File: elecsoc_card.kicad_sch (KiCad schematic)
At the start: 22 parts, among them J1 Conn_01x02_Pin, J2 Conn_01x02_Pin, U1 NA555D

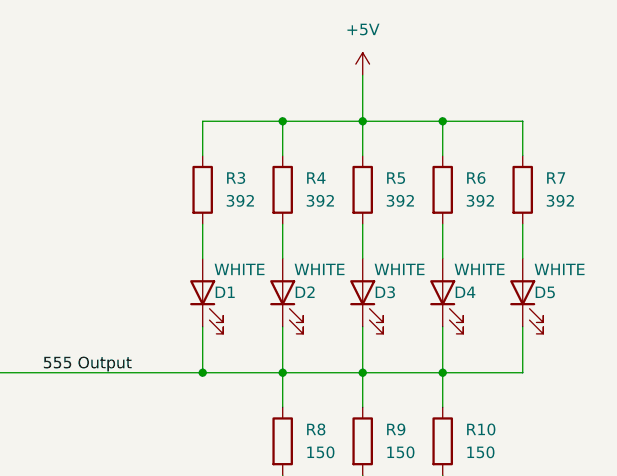
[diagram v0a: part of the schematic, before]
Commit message: Changed R3-R7 to 390
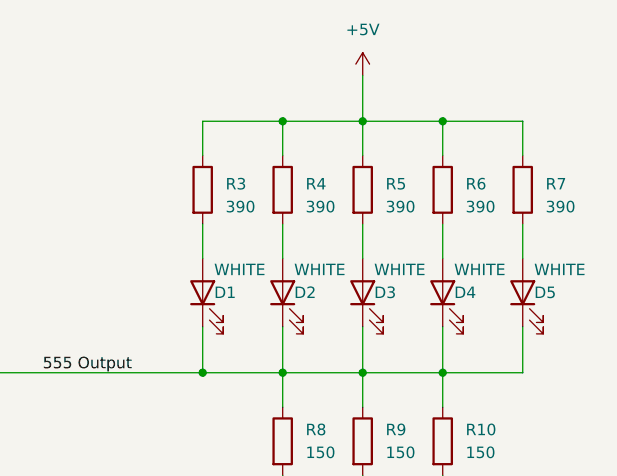
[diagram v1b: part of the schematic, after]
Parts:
- R3, R4, R5, R6, R7: value 392 -> 390
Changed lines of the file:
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@@
   (symbol (lib_id "Device:R") (at 146.05 71.12 0) (unit 1)
     (in_bom yes) (on_board yes) (dnp no) (fields_autoplaced)
-    (property "Reference" "R3" (at 148.59 69.85 0)
-      (effects (font (size 1.27 1.27)) (justify left))
-    )
-    (property "Value" "392" (at 148.59 72.39 0)
+    (property "Reference" "R3" (at 148.59 70.485 0)
+      (effects (font (size 1.27 1.27)) (justify left))
+    )
+    (property "Value" "390" (at 148.59 73.025 0)
       (effects (font (size 1.27 1.27)) (justify left))
     )
@@
   (symbol (lib_id "Device:R") (at 163.83 71.12 0) (unit 1)
     (in_bom yes) (on_board yes) (dnp no) (fields_autoplaced)
-    (property "Reference" "R5" (at 166.37 69.85 0)
-      (effects (font (size 1.27 1.27)) (justify left))
-    )
-    (property "Value" "392" (at 166.37 72.39 0)
+    (property "Reference" "R5" (at 166.37 70.485 0)
+      (effects (font (size 1.27 1.27)) (justify left))
+    )
+    (property "Value" "390" (at 166.37 73.025 0)
       (effects (font (size 1.27 1.27)) (justify left))
     )
@@
   (symbol (lib_id "Device:R") (at 172.72 71.12 0) (unit 1)
     (in_bom yes) (on_board yes) (dnp no) (fields_autoplaced)
-    (property "Reference" "R6" (at 175.26 69.85 0)
-      (effects (font (size 1.27 1.27)) (justify left))
-    )
-    (property "Value" "392" (at 175.26 72.39 0)
+    (property "Reference" "R6" (at 175.26 70.485 0)
+      (effects (font (size 1.27 1.27)) (justify left))
+    )
+    (property "Value" "390" (at 175.26 73.025 0)
       (effects (font (size 1.27 1.27)) (justify left))
     )
@@
   (symbol (lib_id "Device:R") (at 181.61 71.12 0) (unit 1)
     (in_bom yes) (on_board yes) (dnp no) (fields_autoplaced)
-    (property "Reference" "R7" (at 184.15 69.85 0)
-      (effects (font (size 1.27 1.27)) (justify left))
-    )
-    (property "Value" "392" (at 184.15 72.39 0)
+    (property "Reference" "R7" (at 184.15 70.485 0)
+      (effects (font (size 1.27 1.27)) (justify left))
+    )
+    (property "Value" "390" (at 184.15 73.025 0)
       (effects (font (size 1.27 1.27)) (justify left))
     )
@@
   (symbol (lib_id "Device:R") (at 154.94 71.12 0) (unit 1)
     (in_bom yes) (on_board yes) (dnp no) (fields_autoplaced)
-    (property "Reference" "R4" (at 157.48 69.85 0)
-      (effects (font (size 1.27 1.27)) (justify left))
-    )
-    (property "Value" "392" (at 157.48 72.39 0)
-      (effects (font (size 1.27 1.27)) (justify left))
-    )
+    (property "Reference" "R4" (at 157.48 70.485 0)
+      (effects (font (size 1.27 1.27)) (justify left))
+    )
+    (property "Value" "390" (at 157.48 73.025 0)
+      (effects (font (size 1.27 1.27)) (justify left))
+    )

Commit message: SchematicCleanup
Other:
- note added: "Oscillator Circ."
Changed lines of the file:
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@@
     (fill (type none))
   )
-  (text "Frontside USB Connector" (at 34.29 81.28 0)
+  (rectangle (start 77.47 71.12) (end 93.98 109.22)
+    (stroke (width 0) (type default))
+    (fill (type none))
+  )
+  (text "Frontside USB Connector" (at 57.15 81.28 0)
+    (effects (font (size 1.27 1.27)) (justify right bottom))
+  )
+  (text "T = 0.693*(R1+2*R2)*C1\n  = 0.693 * 3 * 4.99k * 47u \n  = 0.487s"
+    (at 66.04 127 0)
     (effects (font (size 1.27 1.27)) (justify left bottom))
   )
-  (text "T = 0.693*(R1+2*R2)*C1\n  = 0.693 * 3 * 4.99k * 47u \n  = 0.487s"
-    (at 66.04 125.73 0)
+  (text "Backside USB Connector" (at 57.15 110.49 0)
+    (effects (font (size 1.27 1.27)) (justify right bottom))
+  )
+  (text "Oscillator\nCirc." (at 93.98 114.3 0)
+    (effects (font (size 1.27 1.27)) (justify right bottom))
+  )
+  (text "Resistors and capacitance values for oscillator" (at 66.04 119.38 0)
     (effects (font (size 1.27 1.27)) (justify left bottom))
   )
-  (text "Backside USB Connector" (at 34.29 110.49 0)
-    (effects (font (size 1.27 1.27)) (justify left bottom))
-  )
-  (text "Resistors and capacitance values for oscillator" (at 66.04 118.11 0)
-    (effects (font (size 1.27 1.27)) (justify left bottom))
-  )

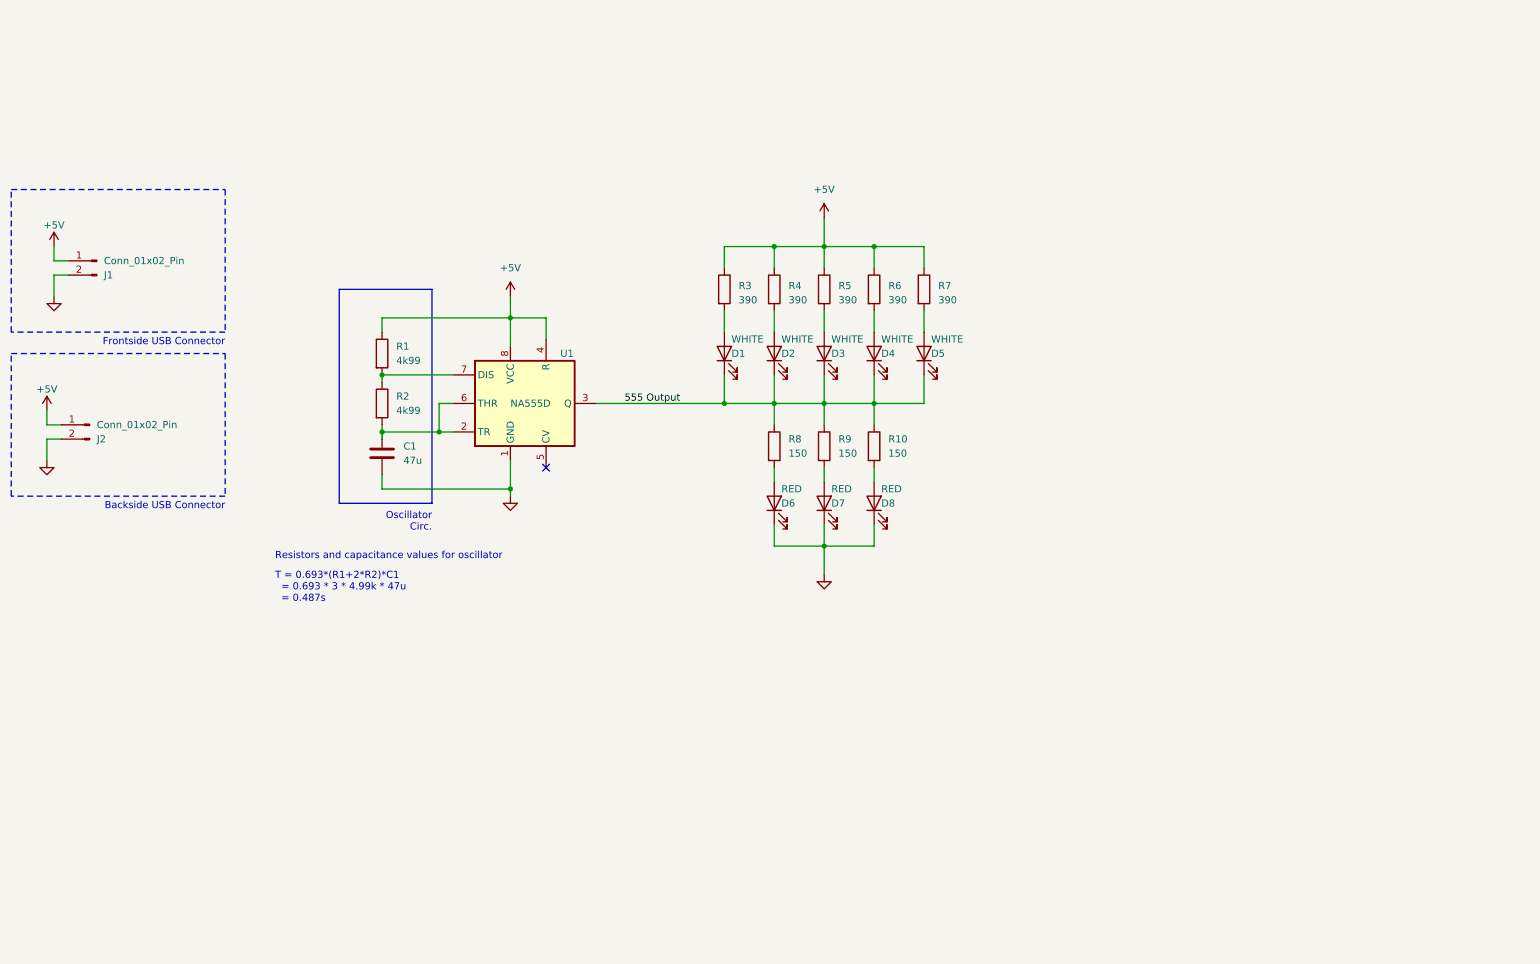
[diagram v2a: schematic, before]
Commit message: Removed Items for Rev2, for Daniel to complete
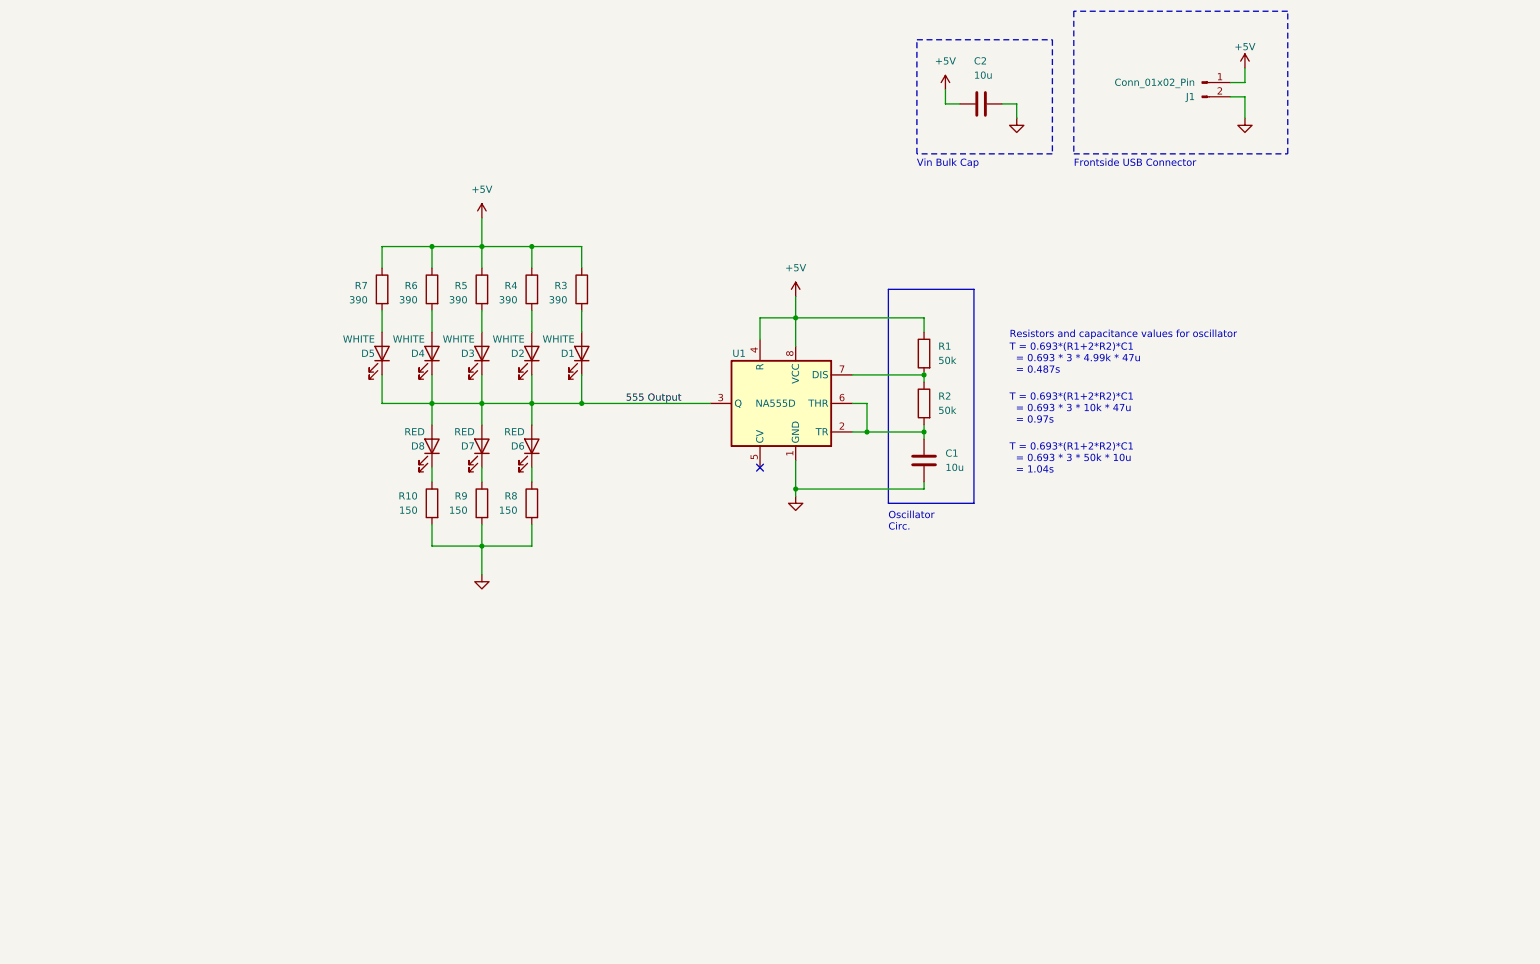
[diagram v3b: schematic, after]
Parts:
- removed J2: Conn_01x02_Pin, Library:USB_A_Male_inboard, symbol Connector:Conn_01x02_Pin
- added C2: 10u, Capacitor_SMD:C_0805_2012Metric_Pad1.18x1.45mm_HandSolder, symbol Device:C
- C1: value 47u -> 10u
- D8: Mfr. No: (none) -> IN-S85AT5UW
- R1, R2: value 4k99 -> 50k
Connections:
- net +5V: now also C2.1
- net 555 Output: now also D6.2 (A), D7.2 (A), D8.2 (A); no longer R10.1, R8.1, R9.1
- net GND: now also R10.2, R8.2, R9.2, C2.2; no longer D6.1 (K), D7.1 (K), D8.1 (K)
- new net: D8.1 (K), R10.1
- new net: D6.1 (K), R8.1
- new net: D7.1 (K), R9.1
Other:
- note added: "T = 0.693*(R1+2*R2)*C1 = 0.693 * 3 * 10k * 47u = 0.97s"
- note added: "T = 0.693*(R1+2*R2)*C1 = 0.693 * 3 * 50k * 10u = 1.04s"
- note added: "Vin Bulk Cap"
- note removed: "Backside USB Connector"
- moved on the sheet: C1, D1, D2, D3, D4, D5, D6, D7, D8, J1, R1, R10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

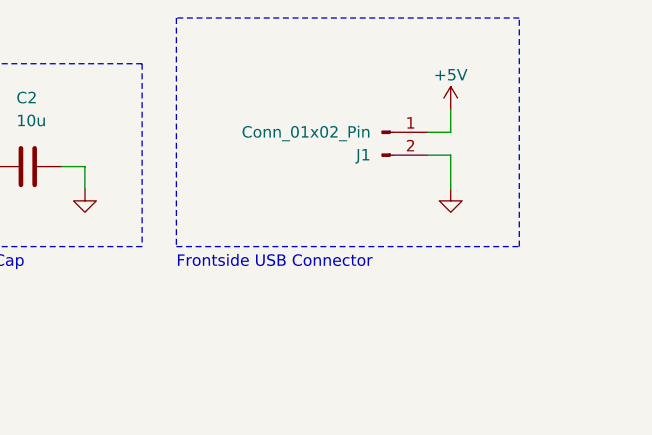
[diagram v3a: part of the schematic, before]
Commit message: Protection resistor and capacitor + cut for 3d printed part
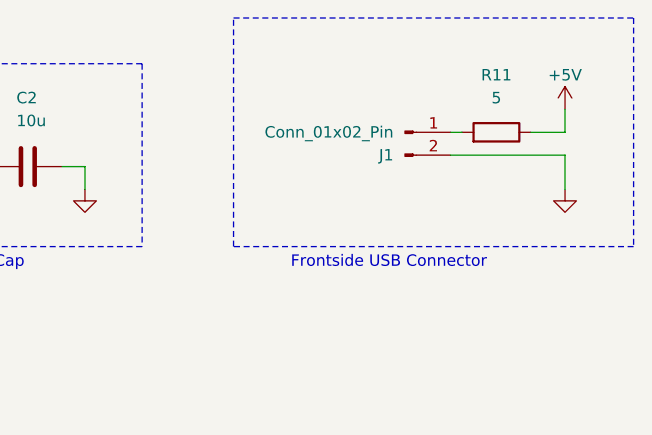
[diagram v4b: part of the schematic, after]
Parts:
- added R11: 5, Resistor_SMD:R_0805_2012Metric_Pad1.20x1.40mm_HandSolder, symbol Device:R
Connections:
- net +5V: now also R11.1; no longer J1.1 (Pin_1)
- new net: J1.1 (Pin_1), R11.2
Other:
- moved on the sheet: J1
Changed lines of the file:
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@@
     (stroke (width 0) (type default))
   )
-  (wire (pts (xy 238.76 36.83) (xy 236.22 36.83))
-    (stroke (width 0) (type default))
-  )
-  (wire (pts (xy 238.76 34.29) (xy 236.22 34.29))
+  (wire (pts (xy 247.65 34.29) (xy 251.46 34.29))
     (stroke (width 0) (type default))
   )
@@
     (stroke (width 0) (type default))
   )
+  (wire (pts (xy 238.76 36.83) (xy 251.46 36.83))
+    (stroke (width 0) (type default))
+  )
   (wire (pts (xy 120.65 91.44) (xy 111.76 91.44))
     (stroke (width 0) (type default))
@@
     (stroke (width 0) (type default))
   )
+  (wire (pts (xy 238.76 34.29) (xy 240.03 34.29))
+    (stroke (width 0) (type default))
+  )
   (wire (pts (xy 158.75 76.2) (xy 152.4 76.2))
     (stroke (width 0) (type default))
@@
     (stroke (width 0) (type default))
   )
-  (wire (pts (xy 238.76 34.29) (xy 238.76 31.75))
+  (wire (pts (xy 251.46 34.29) (xy 251.46 31.75))
     (stroke (width 0) (type default))
   )
@@
     (stroke (width 0) (type default))
   )
-  (wire (pts (xy 238.76 36.83) (xy 238.76 40.64))
+  (wire (pts (xy 251.46 36.83) (xy 251.46 40.64))
     (stroke (width 0) (type default))
   )
@@
     (fill (type none))
   )
-  (rectangle (start 208.28 46.99) (end 246.38 21.59)
+  (rectangle (start 214.63 21.59) (end 259.08 46.99)
     (stroke (width 0) (type dash))
     (fill (type none))
@@
     (fill (type none))
   )
-  (text "Frontside USB Connector" (at 208.28 49.53 0)
+  (text "Frontside USB Connector" (at 220.98 49.53 0)
     (effects (font (size 1.27 1.27)) (justify left bottom))
   )
@@
     )
   )
-  (symbol (lib_id "Connector:Conn_01x02_Pin") (at 231.14 34.29 0) (unit 1)
-    (in_bom yes) (on_board yes) (dnp no)
-    (property "Reference" "J1" (at 229.87 36.83 0)
-      (effects (font (size 1.27 1.27)) (justify right))
-    )
-    (property "Value" "Conn_01x02_Pin" (at 229.87 34.29 0)
-      (effects (font (size 1.27 1.27)) (justify right))
-    )
-    (property "Footprint" "Library:USB_A_Male_inboard" (at 231.14 34.29 0)
-      (effects (font (size 1.27 1.27)) hide)
-    )
-    (property "Datasheet" "~" (at 231.14 34.29 0)
+  (symbol (lib_id "Connector:Conn_01x02_Pin") (at 233.68 34.29 0) (unit 1)
+    (in_bom yes) (on_board yes) (dnp no)
+    (property "Reference" "J1" (at 232.41 36.83 0)
+      (effects (font (size 1.27 1.27)) (justify right))
+    )
+    (property "Value" "Conn_01x02_Pin" (at 232.41 34.29 0)
+      (effects (font (size 1.27 1.27)) (justify right))
+    )
+    (property "Footprint" "Library:USB_A_Male_inboard" (at 233.68 34.29 0)
+      (effects (font (size 1.27 1.27)) hide)
+    )
+    (property "Datasheet" "~" (at 233.68 34.29 0)
       (effects (font (size 1.27 1.27)) hide)
     )
@@
     )
   )
+  (symbol (lib_id "Device:R") (at 243.84 34.29 270) (mirror x) (unit 1)
+    (in_bom yes) (on_board yes) (dnp no) (fields_autoplaced)
+    (property "Reference" "R11" (at 243.84 27.94 90)
+      (effects (font (size 1.27 1.27)))
+    )
+    (property "Value" "5" (at 243.84 30.48 90)
+      (effects (font (size 1.27 1.27)))
+    )
+    (property "Footprint" "Resistor_SMD:R_0805_2012Metric_Pad1.20x1.40mm_HandSolder" (at 243.84 36.068 90)
+      (effects (font (size 1.27 1.27)) hide)
+    )
+    (property "Datasheet" "~" (at 243.84 34.29 0)
+      (effects (font (size 1.27 1.27)) hide)
+    )
+    (pin "1")
+    (pin "2")
+    (instances
+      (project "elecsoc_card"
+        (path "/ec1e128b-e85b-4f54-a1e1-536be465431f"
+          (reference "R11") (unit 1)
+        )
+      )
+    )
+  )
   (symbol (lib_id "Device:R") (at 93.98 71.12 0) (mirror y) (unit 1)
     (in_bom yes) (on_board yes) (dnp no) (fields_autoplaced)
@@
     )
   )
-  (symbol (lib_id "power:+5V") (at 238.76 31.75 0) (mirror y) (unit 1)
-    (in_bom yes) (on_board yes) (dnp no)
-    (property "Reference" "#PWR05" (at 238.76 35.56 0)
-      (effects (font (size 1.27 1.27)) hide)
-    )
-    (property "Value" "+5V" (at 238.76 27.94 0)
+  (symbol (lib_id "power:+5V") (at 251.46 31.75 0) (mirror y) (unit 1)
+    (in_bom yes) (on_board yes) (dnp no)
+    (property "Reference" "#PWR05" (at 251.46 35.56 0)
+      (effects (font (size 1.27 1.27)) hide)
+    )
+    (property "Value" "+5V" (at 251.46 27.94 0)
       (effects (font (size 1.27 1.27)))
     )
-    (property "Footprint" "" (at 238.76 31.75 0)
-      (effects (font (size 1.27 1.27)) hide)
-    )
-    (property "Datasheet" "" (at 238.76 31.75 0)
+    (property "Footprint" "" (at 251.46 31.75 0)
+      (effects (font (size 1.27 1.27)) hide)
+    )
+    (property "Datasheet" "" (at 251.46 31.75 0)
       (effects (font (size 1.27 1.27)) hide)
     )
@@
     )
   )
-  (symbol (lib_id "power:GND") (at 238.76 40.64 0) (mirror y) (unit 1)
-    (in_bom yes) (on_board yes) (dnp no) (fields_autoplaced)
-    (property "Reference" "#PWR06" (at 238.76 46.99 0)
-      (effects (font (size 1.27 1.27)) hide)
-    )
-    (property "Value" "GND" (at 238.76 45.72 0)
-      (effects (font (size 1.27 1.27)) hide)
-    )
-    (property "Footprint" "" (at 238.76 40.64 0)
-      (effects (font (size 1.27 1.27)) hide)
-    )
-    (property "Datasheet" "" (at 238.76 40.64 0)
-      (effects (font (size 1.27 1.27)) hide)
-    )
+  (symbol (lib_id "power:GND") (at 251.46 40.64 0) (mirror y) (unit 1)
+    (in_bom yes) (on_board yes) (dnp no) (fields_autoplaced)
+    (property "Reference" "#PWR06" (at 251.46 46.99 0)
+      (effects (font (size 1.27 1.27)) hide)
+    )
+    (property "Value" "GND" (at 251.46 45.72 0)
+      (effects (font (size 1.27 1.27)) hide)
+    )
+    (property "Footprint" "" (at 251.46 40.64 0)
+      (effects (font (size 1.27 1.27)) hide)
+    )
+    (property "Datasheet" "" (at 251.46 40.64 0)
+      (effects (font (size 1.27 1.27)) hide)
+    )
